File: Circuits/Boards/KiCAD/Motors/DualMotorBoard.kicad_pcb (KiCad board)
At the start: 2 copper layers, 127 x 101.6 mm, 124 parts, among them J1 Conn_01x05, J10 Conn_01x01, J11 Conn_01x01, J12 Conn_01x01, J13 Conn_01x01, J14 Conn_01x01, J15 Conn_01x02, J16 Conn_01x02, J17 MC34063, J2 Conn_01x01, J3 Conn_01x01, J4 Conn_01x01, J5 Conn_01x01, J6 Conn_01x01, J7 Conn_01x01, J8 Conn_01x05, J9 Conn_01x01, Q1 2N3904, Q10 Q_NMOS_DGS, Q11 Q_NMOS_DGS, Q12 Q_NMOS_DGS, Q13 Q_NMOS_DGS, Q14 2N3904, Q15 2N3904, Q16 2N3904, Q17 2N3904, Q18 2N3904, Q19 2N3904, Q2 2N3904, Q20 2N3904, Q21 2N3904, Q22 2N3904, Q23 Q_NMOS_DGS, Q24 Q_NMOS_DGS, Q25 Q_NMOS_DGS, Q26 Q_NMOS_DGS, Q3 2N3904, Q4 2N3904, Q5 2N3904, Q6 2N3904, Q7 2N3904, Q8 2N3904, Q9 2N3904, U2 LM7805_TO220

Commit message: Updated layout errors
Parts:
- moved J10 1.27 mm to (198.1, 30.5)
- moved J13 1.27 mm to (181.6, 30.5)
- moved J3 1.27 mm to (181.6, 30.5)
- moved J6 1.27 mm to (198.1, 30.5)
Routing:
- net GND: track 605.9 -> 609.9 mm
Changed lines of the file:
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@@
     (links 255)
     (no_connects 0)
-    (area 126.281 23.101 254.819 127.549)
+    (area 126.281 24.371 254.819 127.549)
     (thickness 1.6)
     (drawings 4)
-    (tracks 524)
+    (tracks 523)
     (zones 0)
     (modules 124)
@@
   )
   (module Wire_Pads:SolderWirePad_single_2-5mmDrill (layer F.Cu)
-    (at 181.61 29.21)
+    (at 181.61 30.48)
     (fp_text reference J3 (at 0 -5.08) (layer F.SilkS)
       (effects (font (size 1 1) (thickness 0.15)))
@@
   )
   (module Wire_Pads:SolderWirePad_single_2-5mmDrill (layer F.Cu)
-    (at 198.12 29.21)
+    (at 198.12 30.48)
     (fp_text reference J6 (at 0 -5.08) (layer F.SilkS)
       (effects (font (size 1 1) (thickness 0.15)))
@@
   )
   (module Wire_Pads:SolderWirePad_single_2-5mmDrill (layer F.Cu)
-    (at 198.12 29.21)
+    (at 198.12 30.48)
     (fp_text reference J10 (at 0 -5.08) (layer F.SilkS)
       (effects (font (size 1 1) (thickness 0.15)))
@@
   )
   (module Wire_Pads:SolderWirePad_single_2-5mmDrill (layer F.Cu)
-    (at 181.61 29.21)
+    (at 181.61 30.48)
     (fp_text reference J13 (at 0 -5.08) (layer F.SilkS)
       (effects (font (size 1 1) (thickness 0.15)))
@@
     )
   )
-  (gr_line (start 127 127) (end 254 127) (angle 90) (layer Edge.Cuts) (width 0.1))
-  (gr_line (start 127 25.4) (end 254 25.4) (angle 90) (layer Edge.Cuts) (width 0.1))
-  (gr_line (start 127 127) (end 127 25.4) (angle 90) (layer Edge.Cuts) (width 0.1))
+  (gr_line (start 127 25.4) (end 127 127) (angle 90) (layer Edge.Cuts) (width 0.1))
+  (gr_line (start 254 25.4) (end 127 25.4) (angle 90) (layer Edge.Cuts) (width 0.1))
   (gr_line (start 254 127) (end 254 25.4) (angle 90) (layer Edge.Cuts) (width 0.1))
+  (gr_line (start 127 127) (end 254 127) (angle 90) (layer Edge.Cuts) (width 0.1))
   (segment (start 250.19 104.1) (end 243.88 104.1) (width 0.8128) (layer F.Cu) (net 1))
   (segment (start 243.88 104.1) (end 242.65 102.87) (width 0.8128) (layer F.Cu) (net 1))
   (segment (start 242.65 102.87) (end 242.57 102.87) (width 0.8128) (layer F.Cu) (net 1))
   (segment (start 250.19 92.71) (end 250.19 101.6) (width 0.8128) (layer F.Cu) (net 2))
+  (segment (start 214.63 62.23) (end 214.63 63.5) (width 0.8128) (layer B.Cu) (net 3))
+  (segment (start 238.76 57.15) (end 247.65 57.15) (width 0.8128) (layer B.Cu) (net 3))
+  (segment (start 238.76 60.96) (end 238.76 57.15) (width 0.8128) (layer B.Cu) (net 3))
+  (segment (start 236.22 63.5) (end 238.76 60.96) (width 0.8128) (layer B.Cu) (net 3))
+  (segment (start 214.63 63.5) (end 236.22 63.5) (width 0.8128) (layer B.Cu) (net 3))
   (segment (start 170.18 111.76) (end 170.18 114.3) (width 0.8128) (layer B.Cu) (net 3))
   (segment (start 170.18 114.3) (end 168.91 115.57) (width 0.8128) (layer B.Cu) (net 3))
@@
   (segment (start 160.02 101.6) (end 160.02 102.87) (width 0.8128) (layer F.Cu) (net 3))
   (segment (start 149.86 102.87) (end 149.86 101.6) (width 0.8128) (layer F.Cu) (net 3) (status 10))
-  (segment (start 160.02 101.6) (end 160.02 96.52) (width 0.8128) (layer B.Cu) (net 3))
+  (segment (start 160.02 101.6) (end 160.02 96.52) (width 0.8128) (layer B.Cu) (net 3) (status 20))
   (segment (start 160.02 101.6) (end 156.21 101.6) (width 0.8128) (layer F.Cu) (net 3))
   (segment (start 170.18 106.68) (end 170.18 105.41) (width 0.8128) (layer F.Cu) (net 3))
@@
   (segment (start 167.64 60.96) (end 167.64 54.61) (width 0.8128) (layer B.Cu) (net 3))
   (segment (start 168.91 62.23) (end 167.64 60.96) (width 0.8128) (layer B.Cu) (net 3))
-  (segment (start 214.63 62.23) (end 215.9 62.23) (width 0.8128) (layer F.Cu) (net 3))
-  (segment (start 238.76 73.085) (end 239.455 73.66) (width 0.8128) (layer F.Cu) (net 3) (status 20))
-  (segment (start 238.76 67.31) (end 238.76 73.085) (width 0.8128) (layer F.Cu) (net 3))
-  (segment (start 215.9 62.23) (end 217.17 63.5) (width 0.8128) (layer F.Cu) (net 3))
-  (segment (start 217.17 63.5) (end 238.76 63.5) (width 0.8128) (layer F.Cu) (net 3))
-  (segment (start 238.76 63.5) (end 238.76 67.31) (width 0.8128) (layer F.Cu) (net 3))
   (segment (start 247.65 57.15) (end 245.11 53.34) (width 0.8128) (layer F.Cu) (net 3) (status 10))
   (segment (start 239.455 53.34) (end 245.11 53.34) (width 0.8128) (layer F.Cu) (net 3) (status 10))
@@
   (segment (start 162.56 102.87) (end 162.56 101.6) (width 0.8128) (layer B.Cu) (net 20))
   (segment (start 162.56 101.6) (end 162.56 99.06) (width 0.8128) (layer B.Cu) (net 20))
-  (segment (start 162.56 99.06) (end 162.56 96.52) (width 0.8128) (layer B.Cu) (net 20))
+  (segment (start 162.56 99.06) (end 162.56 96.52) (width 0.8128) (layer B.Cu) (net 20) (status 20))
   (segment (start 166.37 115.57) (end 166.37 114.3) (width 0.8128) (layer B.Cu) (net 21))
   (segment (start 167.64 113.03) (end 167.64 111.76) (width 0.8128) (layer B.Cu) (net 21))
@@
   (segment (start 171.45 86.36) (end 171.45 82.55) (width 0.8128) (layer B.Cu) (net 22))
   (segment (start 165.1 90.17) (end 165.1 91.44) (width 0.8128) (layer B.Cu) (net 22))
-  (segment (start 165.1 96.52) (end 165.1 91.44) (width 0.8128) (layer B.Cu) (net 22))
+  (segment (start 165.1 96.52) (end 165.1 91.44) (width 0.8128) (layer B.Cu) (net 22) (status 10))
   (segment (start 171.45 50.8) (end 168.91 50.8) (width 0.8128) (layer B.Cu) (net 22))
   (segment (start 171.45 82.55) (end 171.45 50.8) (width 0.8128) (layer B.Cu) (net 22))
   (segment (start 154.94 93.98) (end 154.94 93.98) (width 0.8128) (layer F.Cu) (net 22) (status 30))
-  (segment (start 165.1 93.98) (end 165.1 96.52) (width 0.8128) (layer F.Cu) (net 22))
+  (segment (start 165.1 93.98) (end 165.1 96.52) (width 0.8128) (layer F.Cu) (net 22) (status 20))
   (segment (start 154.94 93.98) (end 165.1 93.98) (width 0.8128) (layer F.Cu) (net 22) (status 10))
   (segment (start 168.91 50.8) (end 168.91 52.765) (width 0.8128) (layer F.Cu) (net 22))
@@
   (segment (start 193.04 119.38) (end 201.93 119.38) (width 1.27) (layer F.Cu) (net 49))
   (segment (start 195.54 121.92) (end 199.39 121.92) (width 1.27) (layer F.Cu) (net 50))
-  (segment (start 198.12 29.21) (end 198.12 29.21) (width 0.8128) (layer F.Cu) (net 51) (status 30))
+  (segment (start 198.12 31.75) (end 198.12 31.75) (width 0.8128) (layer F.Cu) (net 51) (status 30))
   (segment (start 191.77 93.98) (end 194.31 93.98) (width 1.27) (layer F.Cu) (net 52))
   (zone (net 3) (net_name GND) (layer F.Cu) (hatch edge 0.508)
@@
       (pts
         (xy 234.95 82.55) (xy 218.44 82.55) (xy 218.44 80.01) (xy 214.63 80.01) (xy 214.63 76.2)
-        (xy 208.28 76.2) (xy 208.28 66.04) (xy 234.95 66.04)
+        (xy 208.28 76.2) (xy 208.28 64.77) (xy 234.95 64.77)
       )
     )
@@
       (pts
         (xy 234.95 82.55) (xy 218.44 82.55) (xy 218.44 80.01) (xy 213.36 80.01) (xy 213.36 72.39)
-        (xy 213.36 64.77) (xy 234.95 64.77)
+        (xy 213.36 66.04) (xy 234.95 66.04)
       )
     )

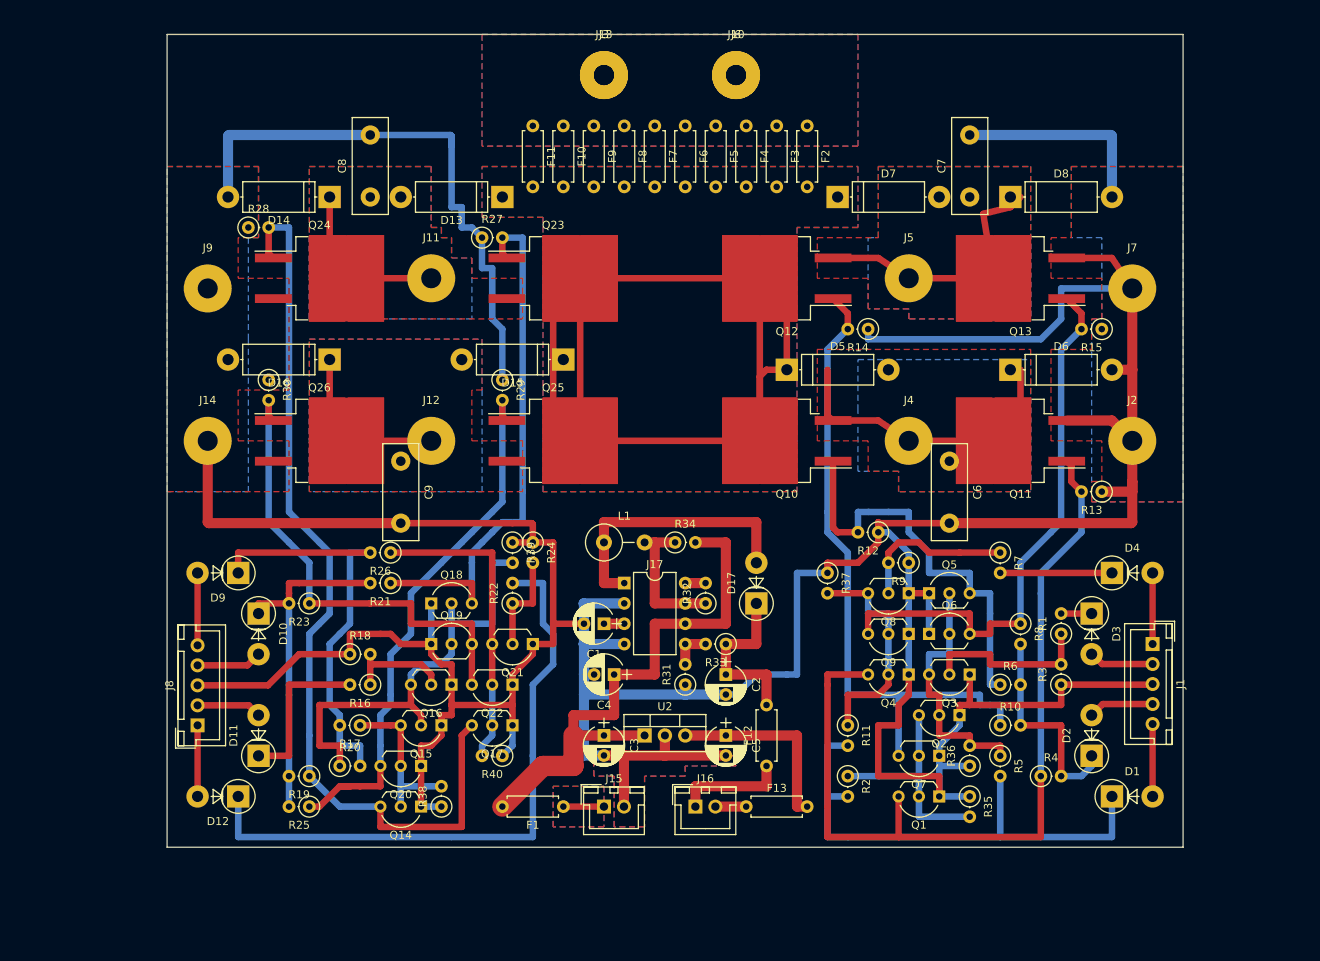
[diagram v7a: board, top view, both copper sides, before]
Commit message: Motor board circuit updated after prototype cut
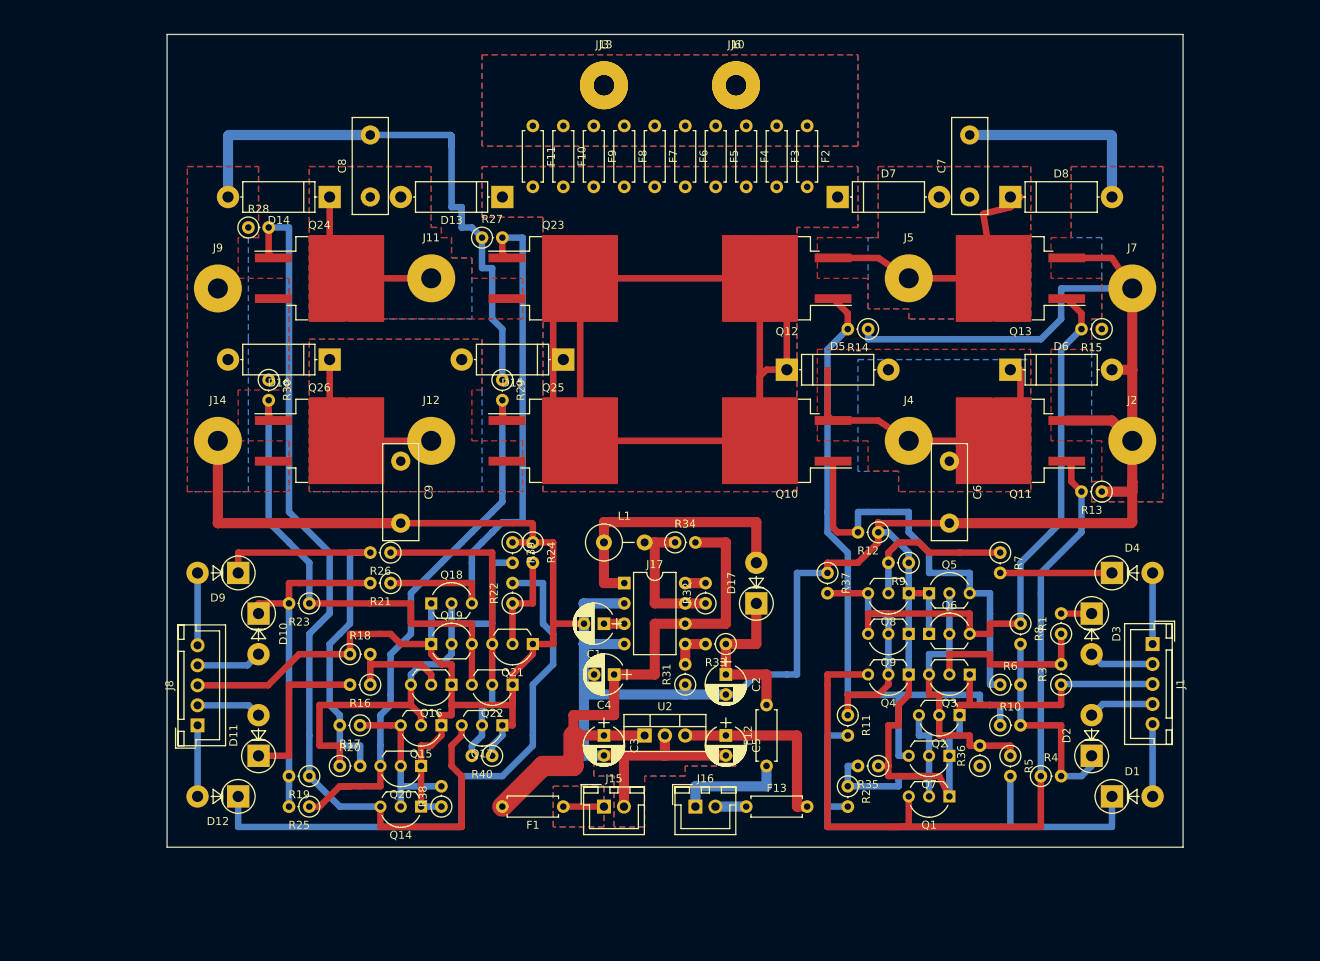
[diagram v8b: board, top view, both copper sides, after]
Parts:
- C4: value 0.33uF -> 100uF
- moved R35 12.0 mm to (215.9, 116.8), turned to 180 degrees
- moved Q17 1.27 mm to (168.9, 111.8)
- moved R11 1.27 mm to (212.1, 110.5)
- moved R40 1.27 mm to (167.6, 115.6)
- moved R5 1.27 mm to (232.4, 115.6)
- moved J10 1.27 mm to (198.1, 31.8)
- moved J13 1.27 mm to (181.6, 31.8)
- moved J3 1.27 mm to (181.6, 31.8)
- moved J6 1.27 mm to (198.1, 31.8)
- moved R2 1.27 mm to (212.1, 119.4)
- moved J14 1.27 mm to (133.3, 76.2)
- moved J9 1.27 mm to (133.3, 57.1)
- moved Q1 1.27 mm to (224.8, 120.7)
- moved Q7 1.27 mm to (224.8, 115.6)
- moved R36 1.27 mm to (228.6, 116.8)
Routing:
- net /MotorControlUnit_2/Speed: track 79.0 -> 74.3 mm
- net GND: track 609.9 -> 605.8 mm
- net /MotorControlUnit_1/DVSW: track 64.8 -> 62.2 mm
- net /MotorControlUnit_1/iSpeed: track 28.5 -> 27.2 mm
- net /MotorControlUnit_1/MFB: track 31.7 -> 33.0 mm
- net /MotorControlUnit_1/MBF: track 82.9 -> 84.1 mm
- net /MotorControlUnit_2/iSpeed: track 38.6 -> 39.9 mm
- net /MotorControlUnit_1/BBM: track 107.0 -> 105.8 mm
- net /MotorControlUnit_1/MBB: track 27.9 -> 27.0 mm
- net /MotorControlUnit_2/BBM: track 114.7 -> 115.2 mm
